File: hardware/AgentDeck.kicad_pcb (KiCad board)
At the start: 4 copper layers, 90 x 90 mm, 98 parts, among them J1 USB-C_SMD-TYPE-C-31-M-12_1, J2 SWD, SW1 CONN-SMD_HOTPLUGPAKAGE__C9900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, SW10 CONN-SMD_HOTPLUGPAKAGE__C9900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, SW11 CONN-SMD_HOTPLUGPAKAGE__C9900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, SW12 CONN-SMD_HOTPLUGPAKAGE__C9900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, SW13 SW-SMD_4P-L5.1-W5.1-P3.70-LS6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, SW14 CONN-SMD_HOTPLUGPAKAGE__C9900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, SW2 CONN-SMD_HOTPLUGPAKAGE__C9900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, SW3 CONN-SMD_HOTPLUGPAKAGE__C9900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, SW4 CONN-SMD_HOTPLUGPAKAGE__C9900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, SW5 CONN-SMD_HOTPLUGPAKAGE__C9900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, SW6 CONN-SMD_HOTPLUGPAKAGE__C9900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, SW7 CONN-SMD_HOTPLUGPAKAGE__C9900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, SW8 CONN-SMD_HOTPLUGPAKAGE__C9900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, SW9 CONN-SMD_HOTPLUGPAKAGE__C9900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, U1 LQFN-56_L7.0-W7.0-P0.4-EP, U2 SOIC-8_L5.3-W5.3-P1.27-LS8.0-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, U3 SOT-223-3_L6.5-W3.4-P2.30-LS7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, U4 SOT-23-5_L3.0-W1.7-P0.95-LS2.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, U6 SOT-23-6_L2.9-W1.6-P0.95-LS2.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, Y1 CRYSTAL-SMD_4P-L3.2-W2.5-BL

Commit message: rename to agentdeck 1.0.0
The product is renamed from ClaudeMicro to AgentDeck for 1.0.0. "Claude" is
Anthropic's trademark and this ships as OSHWA-marked open hardware with the
name on the silk; "Micro" also stopped describing a 150x110 mm V4 deck. Note
AgentDeck collides with an existing project (github.com/puritysb/AgentDeck) -
chosen anyway.

Renamed across board, schematic, netlist, libraries, firmware, host bridge and
docs. Silk reads AGENTDECK and AgentDeck v1.0.0. Generated gerbers under
fab/gerbers are left alone: they are the artifact of the released v0.1.0 and
should be regenerated rather than string-edited.

Also in this commit, all verified 0 errors / 0 unconnected:

- silkscreen pass (tools/silk_pass.py, silk_finish.py, fix_silk_font.py):
  silk_over_copper 79 -> 0, silk_overlap 7 -> 0, text_height 4 -> 0. Silk is
  Red Hat Mono bold; bold and 1.3 mm on the three longest strings are not
  cosmetic - KiCad flags Red Hat Mono Regular at 1.0 mm as insufficient stroke
  weight, the outline-font tradeoff a stroke font avoids. Re-running the pass
  is a no-op, so it is safe after any placement change.

- placement pass (tools/placement_pass.py): three fiducials placed
  asymmetrically >=5 mm from the edges, and C10 moved +0.75/-2.25 mm. C9 and
  C10 were not merely close, their bodies overlapped - two 0603 caps in the
  same space, invisible to DRC because both are +3V3/GND so no clearance rule
  applies. Only C10 moved; the outline and every part the case mates with are
  untouched.

- fab/AgentDeck-BOM-v1.0.0.csv. Records that C22967 is 27k, not the 27R the
  old BOM claimed for the USB series resistors - at 27k USB would not
  enumerate. Correct part is C25190. Also records what LCSC cannot supply:
  the Kailh hot-swap socket (C5333465 discontinued) and the SKQUCAA010
  joystick, plus switches and keycaps which were never LCSC lines.

- docs/img: top and bottom board renders.
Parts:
- added FID1: Fiducial_1mm_Mask2mm, Fiducial_1mm_Mask2mm, F.Cu at (5.95, 9.95)
- added FID2: Fiducial_1mm_Mask2mm, Fiducial_1mm_Mask2mm, F.Cu at (81.0, 5.95)
- added FID3: Fiducial_1mm_Mask2mm, Fiducial_1mm_Mask2mm, F.Cu at (21.9, 85.0)
- moved C10 2.37 mm to (37.2, 85.2)
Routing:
- net +3V3: track 137.5 -> 138.5 mm
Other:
- board text added: "AGENTDECK"
- board text added: "AgentDeck v1.0.0 · OSHW · CERN-OHL-S v2 · github.com/Brillar0101"
- board text removed: "CLAUDE MICRO"
- board text removed: "ClaudeMicro v0.1 · OSHW · CERN-OHL-S v2 · github.com/Brillar0101"

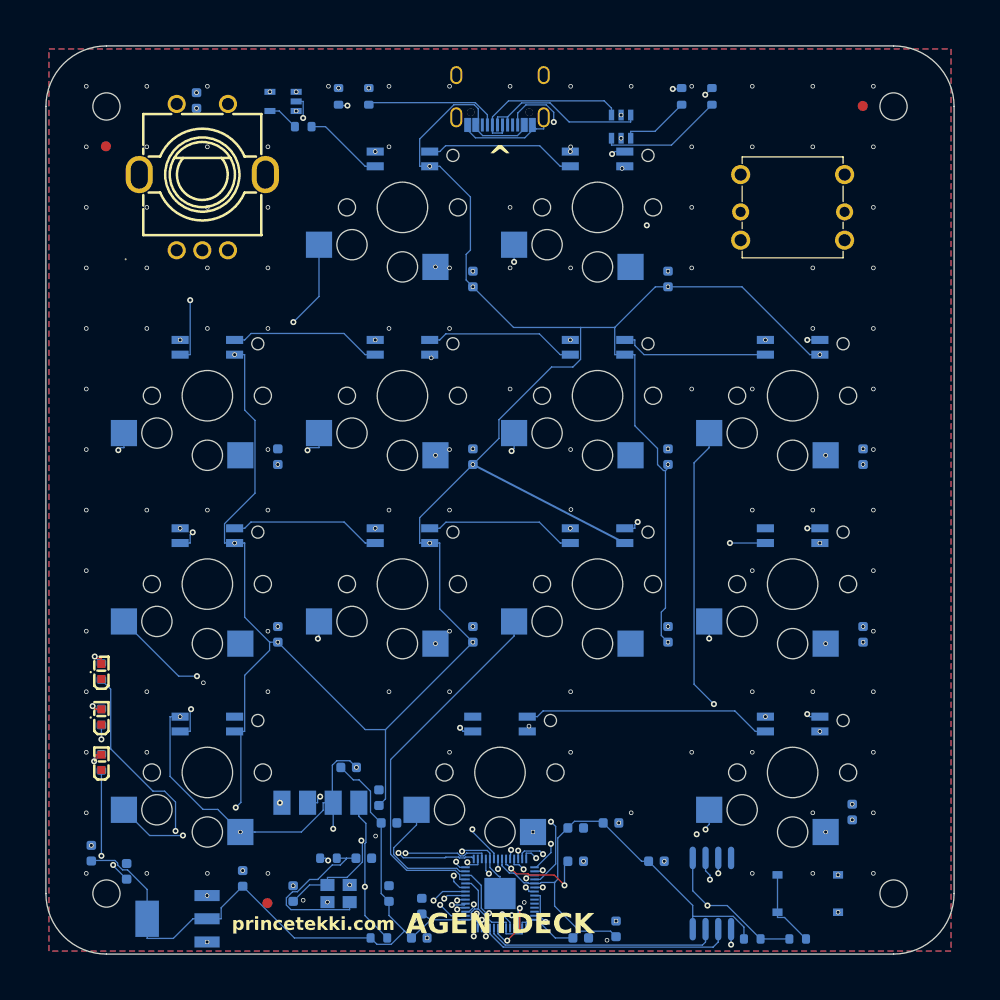
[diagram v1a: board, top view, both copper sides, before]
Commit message: grow board to 95mm
Board 95.1x95.1 (was 90x90): outline +2.5mm/side, corner arcs r6 preserved.
MH1-4 moved to (3.086,3.086)+mirrors, M2.5 confirmed (BOM corrected from M2).
J1 USB-C moved to y=2.87, face 0.15mm inside the new edge. U1 down 2mm to (45,86).
All pours expanded to -2.20..92.20. Full reroute with freerouting 2.3.0
(2.2.4 hangs; 2.3.0 fixes it - #739). DRC: 0 errors, 42 warnings.

KNOWN OPEN (2 ratsnest lines, fix by hand in pcbnew):
 - U1 pin 19 (TESTEN->GND): dogleg laid at (44.0,82.57)->(43.66,84.85) into EP
   but the pad does not register touching tracks; verify/redraw in GUI.
 - U1 pin 10 (IOVDD): unrouted; via-blocked cage (K1/K5 In1, K8/K9 B.Cu,
   K6 diag). +3V3 F.Cu bridge passes overhead at x~41.4 for a GUI hookup.

Case regenerated parametrically (enclosure/src/generate_case.py, new):
100.2mm shells, M2.5 button-head + heat-set stack, 14mm flared USB slot,
LED windows, BOOTSEL pinhole. Old non-manifold STLs replaced (0 bad edges).
Blender assembly updated; Lucide icons on caps; docs to 95x95.
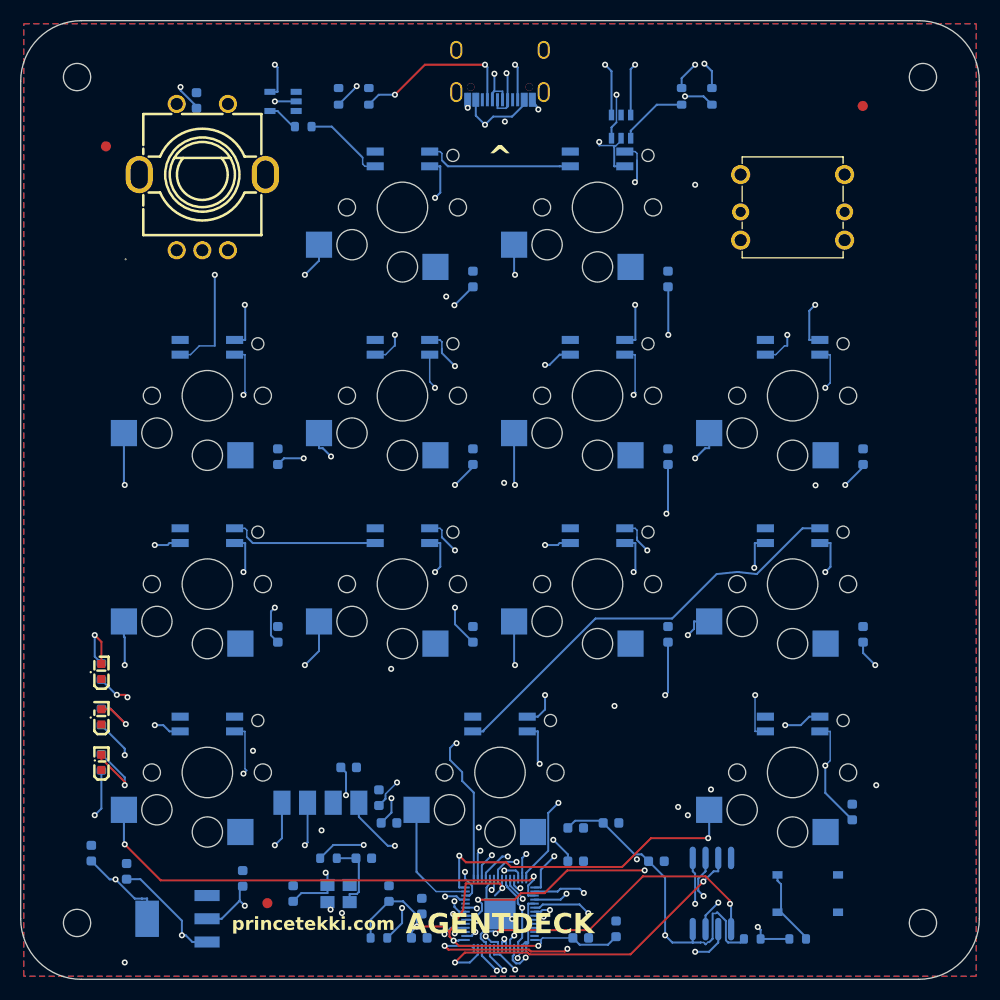
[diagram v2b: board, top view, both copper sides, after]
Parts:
- C1, C2: value C_0603_1608Metric -> 15pF
- C10, C11, C12, C15, C19, C20, C21, C22, C23, C24, C25, C26, C27, C28, C29, C3, C30, C31, C5, C6, C7, C8, C9: value C_0603_1608Metric -> 100nF
- C13, C14: value C_0603_1608Metric -> 1uF
- C16, C17: value C_0603_1608Metric -> 10uF
- D1, D10, D11, D12, D13, D14, D15, D2, D3, D4, D5, D6: value LED-SMD_4P-L3.2-W2.8-LS5.9_SK6812MINI-E -> SK6812MINI-E
- D7, D8, D9: value LED-SMD_L1.6-W0.8-R-RD -> red
- ENC1: value SW-TH_EC11E1820402 -> EC11
- J1: value USB-C_SMD-TYPE-C-31-M-12_1 -> USB-C
- KEY1, KEY10, KEY11, KEY12, KEY14, KEY2, KEY3, KEY4, KEY5, KEY6, KEY7, KEY8, KEY9: footprint (none) -> AgentDeck:KeyOutline
- MH1, MH2, MH3, MH4: footprint (none) -> AgentDeck:MountingHole_M2.5
- R1, R2: value R_0603_1608Metric -> 5.1k
- R10, R11, R12, R5, R7: value R_0603_1608Metric -> 1k
- R3, R4: value R_0603_1608Metric -> 27R
- R6: value R_0603_1608Metric -> 10k DNP
- R8: value R_0603_1608Metric -> 10k
- R9: value R_0603_1608Metric -> 330R
- SW1: value CONN-SMD_HOTPLUGPAKAGE__C9900010116 -> K1
- SW10: value CONN-SMD_HOTPLUGPAKAGE__C9900010116 -> K10
- SW11: value CONN-SMD_HOTPLUGPAKAGE__C9900010116 -> K11
- SW12: value CONN-SMD_HOTPLUGPAKAGE__C9900010116 -> K12
- SW13: value SW-SMD_4P-L5.1-W5.1-P3.70-LS6.5-TL_H1.5 -> BOOTSEL
- SW2: value CONN-SMD_HOTPLUGPAKAGE__C9900010116 -> K2
- SW3: value CONN-SMD_HOTPLUGPAKAGE__C9900010116 -> K3
- SW4: value CONN-SMD_HOTPLUGPAKAGE__C9900010116 -> K4
- SW5: value CONN-SMD_HOTPLUGPAKAGE__C9900010116 -> K5
- SW6: value CONN-SMD_HOTPLUGPAKAGE__C9900010116 -> K6
- SW7: value CONN-SMD_HOTPLUGPAKAGE__C9900010116 -> K7
- SW8: value CONN-SMD_HOTPLUGPAKAGE__C9900010116 -> K8
- SW9: value CONN-SMD_HOTPLUGPAKAGE__C9900010116 -> K9
- U1: value LQFN-56_L7.0-W7.0-P0.4-EP -> RP2040
- U2: value SOIC-8_L5.3-W5.3-P1.27-LS8.0-BL -> W25Q128JVSIQ
- U3: value SOT-223-3_L6.5-W3.4-P2.30-LS7.0-BR -> AMS1117-3.3
- U4: value SOT-23-5_L3.0-W1.7-P0.95-LS2.8-BR -> 74AHCT1G125
- U6: value SOT-23-6_L2.9-W1.6-P0.95-LS2.8-BL -> USBLC6-2SC6
- Y1: value CRYSTAL-SMD_4P-L3.2-W2.5-BL -> ABM8-272-T3
- moved MH4 4.12 mm to (86.9, 86.9)
- moved MH2 4.12 mm to (86.9, 3.09)
- moved MH3 4.12 mm to (3.09, 86.9)
- moved MH1 4.12 mm to (3.09, 3.09)
- moved J1 2.50 mm to (45.0, 2.87)
- moved U1 2.00 mm to (45.0, 86.0)
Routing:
- net GND: track 156.0 -> 6.48 mm, vias 159 -> 5
- net VBUS: track 278.2 -> 131.5 mm, vias 27 -> 28
- net +3V3: track 138.5 -> 182.3 mm, vias 0 -> 11
- net K3: track 64.4 -> 89.9 mm, vias 2 -> 3
- net LED_D7: track 72.2 -> 94.4 mm, vias 2 -> 3
- net AUX1: track 59.1 -> 79.3 mm, vias 2 -> 4
- net LED_DATA: track 89.9 -> 108.3 mm, vias 2 -> 3
- net QSPI_SD3: track 23.4 -> 38.5 mm, vias 0 -> 2
- net JOY_CTR: track 82.2 -> 95.3 mm, vias 1 -> 2
- net K8: track 32.8 -> 45.7 mm, vias 2 -> 3
- net ENC_A: track 76.7 -> 88.4 mm, vias 1 -> 2
- net K7: track 46.8 -> 58.5 mm, vias 2 -> 3
- net LED_D13: track 67.4 -> 78.5 mm
- net XOUT_XTAL: track 17.4 -> 7.15 mm
- net USB_DM: track 92.4 -> 102.0 mm
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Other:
- board size 90 x 90 mm -> 95 x 95 mm

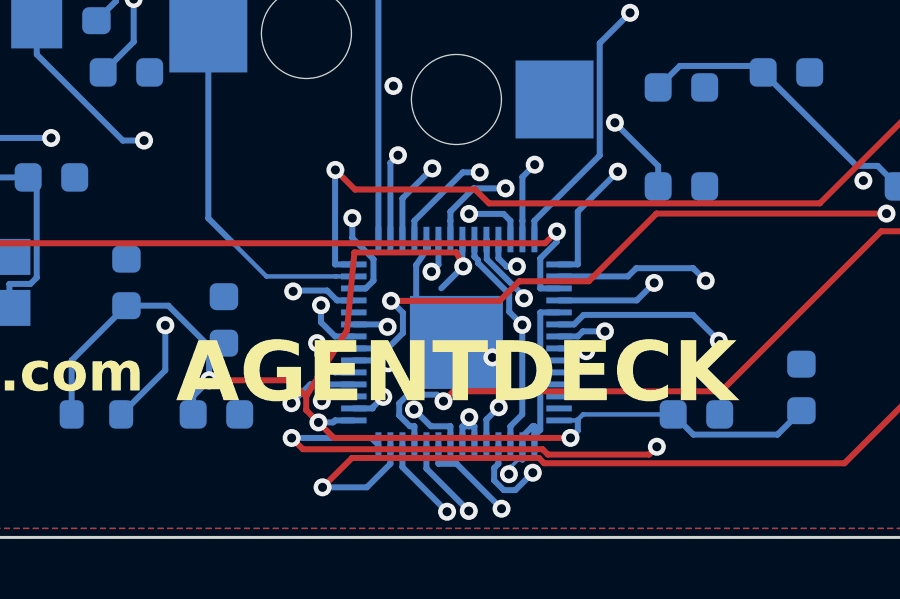
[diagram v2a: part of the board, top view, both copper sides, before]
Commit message: stitch gnd add pour hookup
Pour-aware EP stitch via chain (pad19->dogleg->EP->via->In1 pour, all links
verified by the connectivity API) plus a direct B.Cu run into verified pour
copper. kicad-cli still reports the pad19 ratsnest line (its refill may
differ from the saved fill - verify in pcbnew GUI, likely phantom).
Pad 10 (+3V3) remains genuinely unrouted: via-caged on all four layers;
the F.Cu +3V3 bridge passes over the pad at x~41.4 as the GUI hookup point.
DRC: 0 errors, 42 warnings, 2 unconnected items.
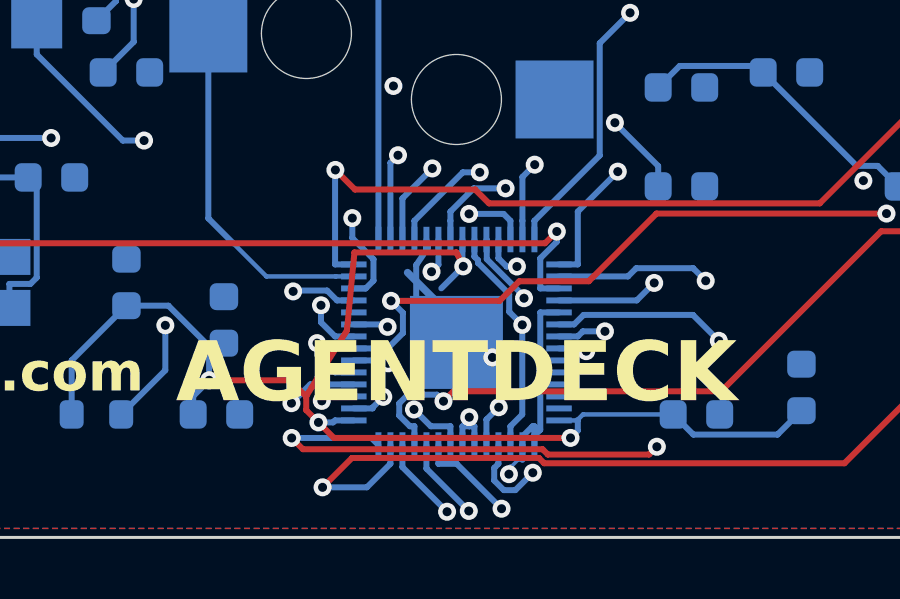
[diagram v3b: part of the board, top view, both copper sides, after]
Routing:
- net GND: track 6.48 -> 10.5 mm
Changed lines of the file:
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@@
+	)
+	(segment
+		(start 46.2 86.5)
+		(end 43.371572 83.671572)
+		(width 0.25)
+		(layer "B.Cu")
+		(net "GND")
 	)
 	(segment
